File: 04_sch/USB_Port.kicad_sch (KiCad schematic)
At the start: 12 parts, among them J4 USB_B_Micro, Q2 SS8050-G, Q3 SS8050-G, U6 CP2102N-Axx-xQFN28

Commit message: Fix tantalum capacitor & JLCPCB codes
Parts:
- C20, C21, C22: LCSC (none) -> C15850
- C23: LCSC (none) -> C49678
- D7: LCSC (none) -> C124187
- R17: LCSC (none) -> C17513
- R18, R19: LCSC (none) -> C191101
- U6: LCSC (none) -> C964632
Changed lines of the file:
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@@
 			)
 		)
-		(property "LCSC" ""
+		(property "LCSC" "C124187"
 			(at 133.35 67.31 0)
 			(effects
@@
 			)
 		)
-		(property "LCSC" ""
+		(property "LCSC" "C964632"
 			(at 166.37 93.98 0)
 			(effects
@@
 			)
 		)
-		(property "LCSC" ""
+		(property "LCSC" "C17513"
 			(at 148.59 62.23 0)
 			(effects
@@
 			)
 		)
-		(property "LCSC" ""
+		(property "LCSC" "C15850"
 			(at 129.54 62.23 0)
 			(effects
@@
 			)
 		)
-		(property "LCSC" ""
+		(property "LCSC" "C15850"
 			(at 168.91 55.88 0)
 			(effects
@@
 			)
 		)
-		(property "LCSC" ""
+		(property "LCSC" "C15850"
 			(at 168.91 48.26 0)
 			(effects
@@
 			)
 		)
-		(property "LCSC" ""
+		(property "LCSC" "C191101"
 			(at 120.65 151.13 0)
 			(effects
@@
 			)
 		)
-		(property "LCSC" ""
+		(property "LCSC" "C191101"
 			(at 120.65 135.89 0)
 			(effects
@@
 			)
 		)
-		(property "LCSC" ""
+		(property "LCSC" "C49678"
 			(at 140.97 72.39 0)
 			(effects

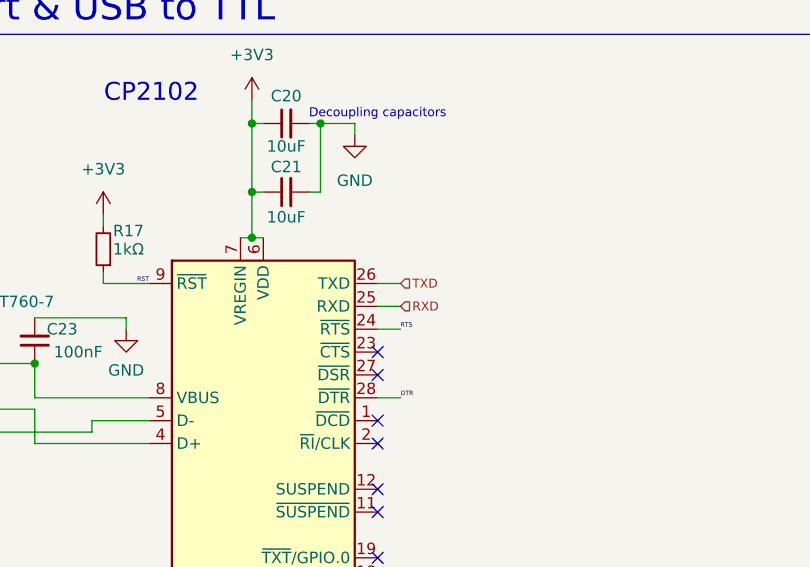
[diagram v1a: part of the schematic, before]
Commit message: Fix CP2102 connection
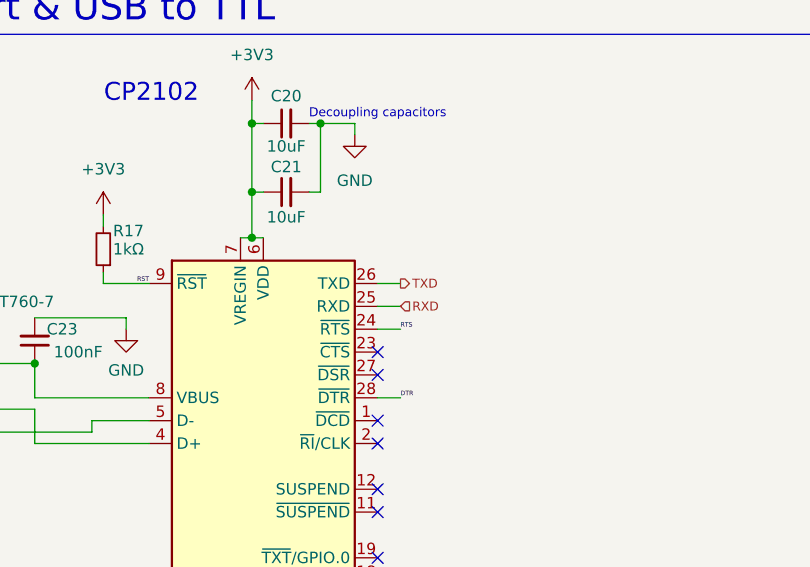
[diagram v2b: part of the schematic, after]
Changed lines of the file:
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@@
 	)
 	(hierarchical_label "TXD"
-		(shape input)
+		(shape output)
 		(at 181.61 66.04 0)
 		(fields_autoplaced yes)
